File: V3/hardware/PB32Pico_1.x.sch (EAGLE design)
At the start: 26 parts, among them IC1 ESP32-PICO-D4UM-ESP32-PICO-D4, U1 AP2112K-3.3TRG1

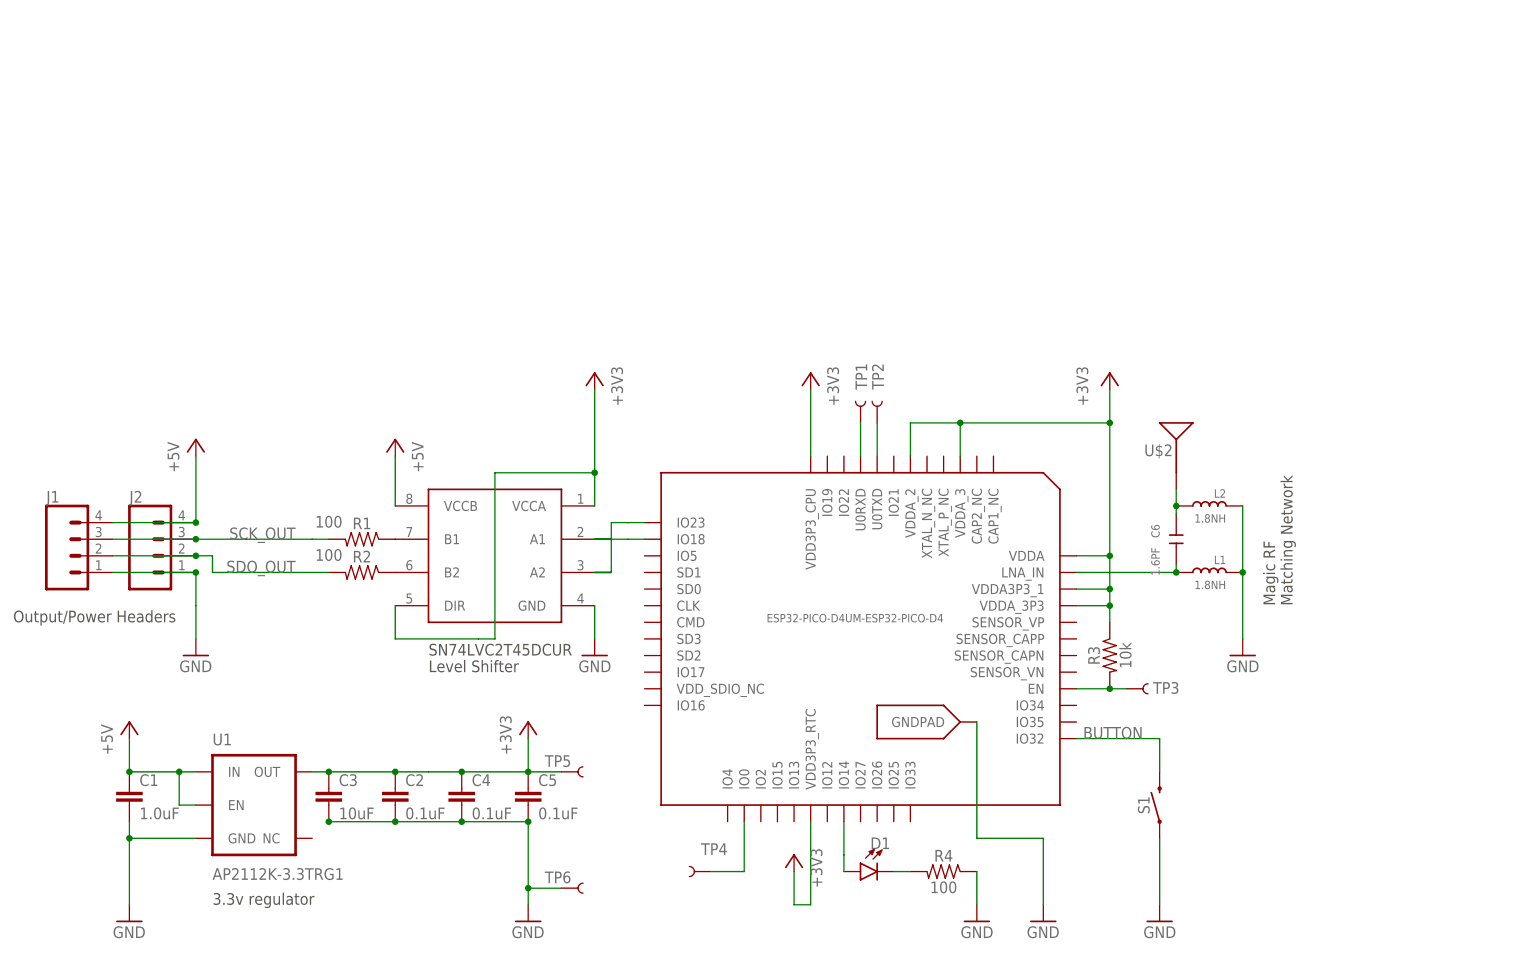
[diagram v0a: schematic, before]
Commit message: PICO pcb reworked
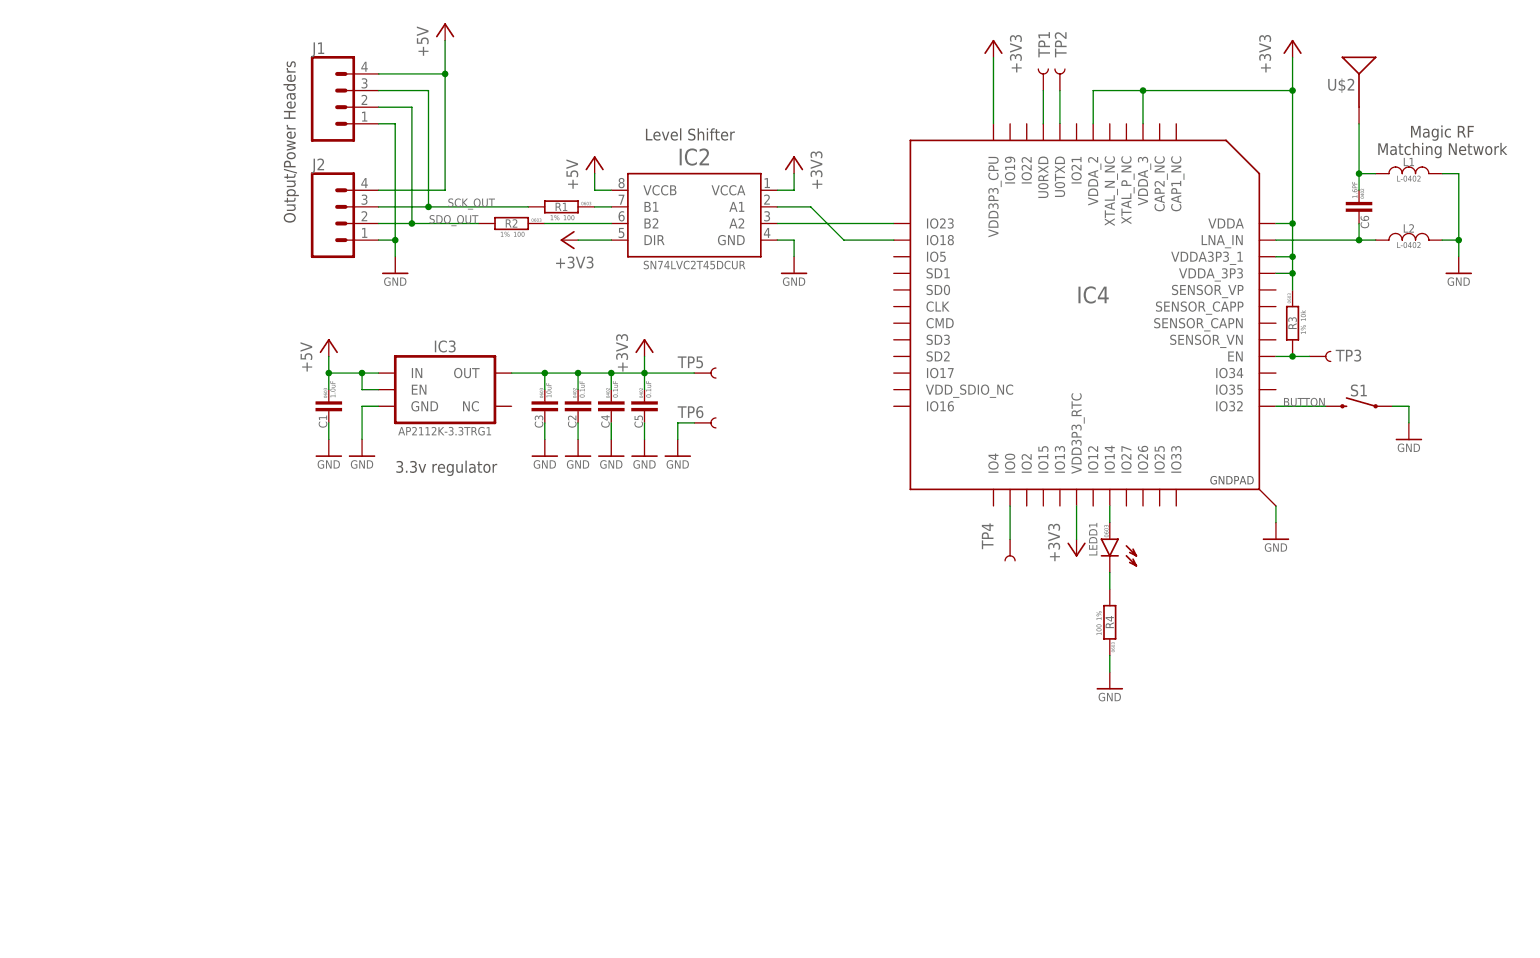
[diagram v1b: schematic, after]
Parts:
- removed D1: (no value), SparkFun-LED:LED0603
- removed IC1: ESP32-PICO-D4UM-ESP32-PICO-D4, bens:ESP32-PICO-D4UM-ESP32-PICO-D4
- removed U$1: SN74LVC2T45DCUR, SOP50P310X90-8N:SN74LVC2T45DCUR
- removed U1: AP2112K-3.3TRG1, SparkFun-PowerIC:V_REG_AP2112K-3.3V
- added IC2: SN74LVC2T45DCUR, pixelblaze:SN74LVC2T45DCUR
- added IC3: 3.3V, pixelblaze:V_REG_AP2112K-3.3V
- added IC4: ESP32-PICO-D4UM-ESP32-PICO-D4, pixelblaze:ESP32-PICO-D4UM-ESP32-PICO-D4
- added LEDD1: LED-0603, rc:LED-0603
- C1: device SparkFun-Capacitors:1.0UF-0603-16V-10% -> rc:C-0603
- C2, C4, C5: device SparkFun-Capacitors:0.1UF-0402-16V-10% -> rc:C-0402
- C3: device SparkFun-Capacitors:10UF-0603-6.3V-20% -> rc:C-0603
- C6: device Seeed-Capacitor:CERAMIC-1.5PF-50V-0.1PF-NPO(0402) -> rc:C-0402
- L1: value 1.8NH -> L-0402; device Seeed-Inductor:SMD-INDUCTOR-3.3NH-0.3NH-300MA(0402) -> rc:L-0402
- L2: value 1.8NH -> L-0402; device Seeed-Inductor:SMD-INDUCTOR-4.7NH-0.3NH-300MA(0402) -> rc:L-0402
- R1, R2, R4: device SparkFun-Resistors:100OHM-0603-1/10W-1% -> rc:R-1%-0603
- R3: device SparkFun-Resistors:10KOHM-0603-1/10W-1% -> rc:R-1%-0603
- S1: device SparkFun-Switches:MOMENTARY-SWITCH-SPST-SMD-5.2MM -> pixelblaze:MOMENTARY-SWITCH-SPST-SMD-5.2MM
- U$2: device bens:CHIP-ANTENNASHORT -> pixelblaze:CHIP-ANTENNASHORT
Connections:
- net +3V3: now also IC2.DIR, IC2.VCCA, IC3.OUT, IC4.VDD3P3_CPU, IC4.VDD3P3_RTC, IC4.VDDA, IC4.VDDA3P3_1, IC4.VDDA_2, IC4.VDDA_3, IC4.VDDA_3P3; no longer IC1G$1.VDD3P3_CPU, IC1G$1.VDD3P3_RTC, IC1G$1.VDDA, IC1G$1.VDDA3P3_1, IC1G$1.VDDA_2, IC1G$1.VDDA_3, IC1G$1.VDDA_3P3, U$1.DIR, U$1.VCCA, U1.OUT
- net +5V: now also IC2.VCCB, IC3.EN, IC3.IN; no longer U$1.VCCB, U1.EN, U1.IN
- net BUTTON: now also IC4.IO32; no longer IC1G$1.IO32
- net EN: now also IC4.EN; no longer IC1G$1.EN
- net GND: now also IC2.GND, IC3.GND, IC4.GNDPAD, L1.P$2, L2.P$2; no longer IC1G$2.GNDPAD, L1.1, L2.1, U$1.GND, U1.GND
- net IO0: now also IC4.IO0; no longer IC1G$1.IO0
- net N$1: now also L1.P$1; no longer L2.2
- net N$2: now also IC4.IO14, LEDD1.A; no longer D1.A, IC1G$1.IO14
- net N$3: now also LEDD1.C; no longer D1.C
- net N$4: now also IC2.B1; no longer U$1.B1
- net N$5: now also IC2.B2; no longer U$1.B2
- net N$6: now also IC4.LNA_IN, L2.P$1; no longer IC1G$1.LNA_IN, L1.2
- net SCK: now also IC2.A1, IC4.IO18; no longer IC1G$1.IO18, U$1.A1
- net SDO: now also IC2.A2, IC4.IO23; no longer IC1G$1.IO23, U$1.A2
- net U0TX: now also IC4.U0TXD; no longer IC1G$1.U0TXD
- net UORX: now also IC4.U0RXD; no longer IC1G$1.U0RXD
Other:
- note removed: "SN74LVC2T45DCUR"
- moved on the sheet: J1, J2, S1, TP1, TP2, TP3, TP4, TP5, TP6, U$2
